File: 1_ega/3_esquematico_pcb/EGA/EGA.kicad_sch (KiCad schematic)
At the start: 46 parts, among them J1 Entrada de 12V, J10 M1, J11 M2, J12 IN1 IN2 EN, J13 OUT, J14 I2C, J15 12, J16 5, J17 UART, J18 SW DT CLK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

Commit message: Archivo de KiCad final
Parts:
- removed J12: IN1 IN2 EN, Connector_PinHeader_2.54mm:PinHeader_1x03_P2.54mm_Vertical, symbol Connector:Conn_01x03_Pin
- removed J14: I2C, Connector_PinHeader_2.54mm:PinHeader_2x01_P2.54mm_Vertical, symbol Connector:Conn_01x02_Pin
- removed J17: UART, Connector_PinHeader_2.54mm:PinHeader_2x01_P2.54mm_Vertical, symbol Connector:Conn_01x02_Pin
- removed J18: SW DT CLK, Connector_PinHeader_2.54mm:PinHeader_1x03_P2.54mm_Vertical, symbol Connector:Conn_01x03_Pin
- removed J19: SPI, Connector_PinHeader_2.54mm:PinHeader_1x04_P2.54mm_Vertical, symbol Connector:Conn_01x04_Pin
- removed J20: LEDS, Connector_PinHeader_2.54mm:PinHeader_2x01_P2.54mm_Vertical, symbol Connector:Conn_01x02_Pin
- removed J21: BOTONES, Connector_PinHeader_2.54mm:PinHeader_2x01_P2.54mm_Vertical, symbol Connector:Conn_01x02_Pin
- removed J22, J23, J24: GND, Connector_PinHeader_2.54mm:PinHeader_1x03_P2.54mm_Vertical, symbol Connector:Conn_01x03_Pin
- added C5: 100uF, Capacitor_THT:CP_Radial_D7.5mm_P2.50mm, symbol Device:C_Polarized
- added J14: GND, Connector_PinHeader_2.54mm:PinHeader_1x01_P2.54mm_Vertical, symbol Connector:Conn_01x01_Pin
- added J17: EnB, Connector_PinHeader_2.54mm:PinHeader_1x01_P2.54mm_Vertical, symbol Connector:Conn_01x01_Pin
- C1: value 0,22uF -> 0,1uF
- J8, J9: footprint Connector_PinHeader_2.54mm:PinHeader_1x03_P2.54mm_Vertical -> Connector_PinSocket_2.54mm:PinSocket_1x03_P2.54mm_Vertical
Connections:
- net +12V: now also C5.1
- net +3.3V: no longer J3.3 (Pin_3)
- net +5V: now also J3.3 (Pin_3)
- net CLK: now also A1.15 (GPIO11); no longer A1.17 (GPIO13)
- net DT: now also A1.14 (GPIO10); no longer A1.16 (GPIO12)
- net EnB: now also J17.1 (Pin_1)
- net GND: now also C5.2, J14.1 (Pin_1)
- net IN3: now also R1.1
- net IN4: now also R2.2
- net SCL: no longer J8.2 (Pin_2)
- net SDA: no longer J8.3 (Pin_3)
- net SW: now also A1.12 (GPIO9); no longer A1.15 (GPIO11)
- net UART RX: now also A1.17 (GPIO13); no longer A1.22 (GPIO17)
- net UART TX: now also A1.16 (GPIO12); no longer A1.21 (GPIO16)
- net BC: no longer names the net of A1.19 (GPIO14), SW2.1
- net BS: no longer names the net of A1.20 (GPIO15), SW1.1
- removed net LEDA: A1.14 (GPIO10), R2.2
- removed net LEDH: A1.12 (GPIO9), R1.1
- new net SCL_EGB: A1.22 (GPIO17), J8.2 (Pin_2)
- new net SDA_EGB: A1.21 (GPIO16), J8.3 (Pin_3)
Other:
- moved on the sheet: A1, C1, C2, D1, D2, J13, J25, R1, R2, SW1, SW2, U1

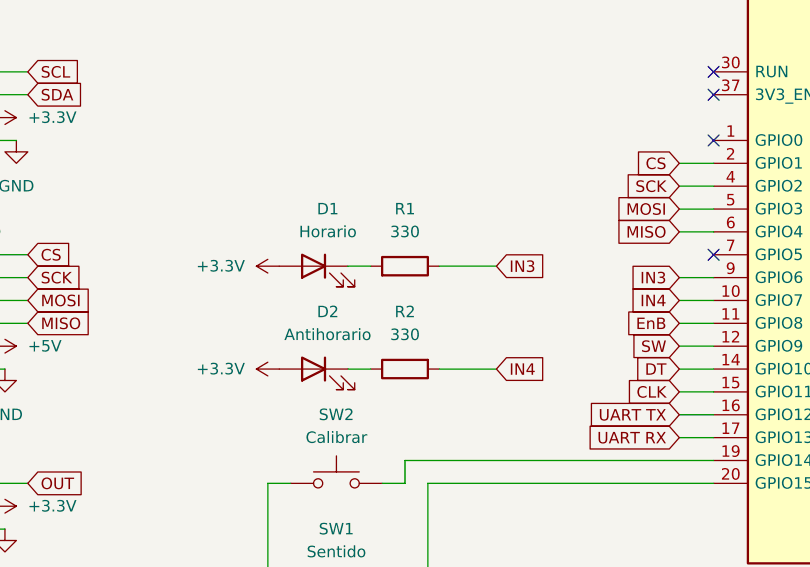
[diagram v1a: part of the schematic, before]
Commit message: Cambio en R1 y R2
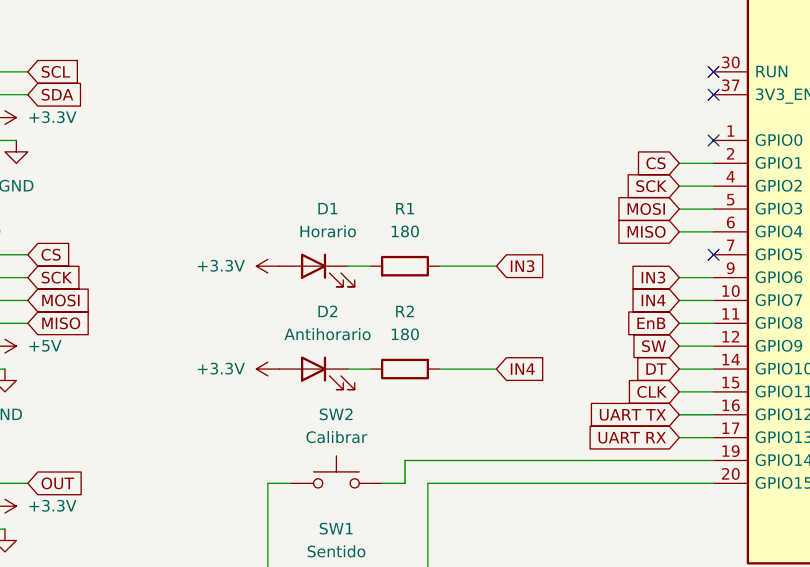
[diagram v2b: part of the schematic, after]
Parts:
- R1, R2: value 330 -> 180
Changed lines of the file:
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@@
 			)
 		)
-		(property "Value" "330"
+		(property "Value" "180"
 			(at 72.39 107.95 90)
 			(effects
@@
 			)
 		)
-		(property "Value" "330"
+		(property "Value" "180"
 			(at 72.39 96.52 90)
 			(effects
